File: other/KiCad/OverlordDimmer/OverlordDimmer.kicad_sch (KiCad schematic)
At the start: 61 parts, among them J1 Connector_Screw_Terminal_01x09, J2 USB_cable, J3 RJ45x2, J4 Connector_Screw_Terminal_01x09, J5 USB_B, J6 Conn_01x12_Female, Q21 2N7002E, Q22 2N7002E, Q43 NPN, Q44 BC817, Q45 NPN, U12 4N35, U4 SN65HVD230

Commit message: Finalised ver1.0 revA of PCB
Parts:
- added D18: SBR1A40S1, Diode_SMD:D_SOD-123, symbol Device:D
- Q43, Q45: value NPN -> 2SC4061KT146N
- R12, R13: footprint Resistor_SMD:R_1812_4532Metric_Pad1.30x3.40mm_HandSolder -> Resistor_SMD:R_0402_1005Metric_Pad0.72x0.64mm_HandSolder
- R15, R27: footprint Resistor_SMD:R_0805_2012Metric_Pad1.20x1.40mm_HandSolder -> Resistor_SMD:R_0402_1005Metric_Pad0.72x0.64mm_HandSolder
- R56: footprint Resistor_SMD:R_1210_3225Metric_Pad1.30x2.65mm_HandSolder -> Resistor_SMD:R_0805_2012Metric_Pad1.20x1.40mm_HandSolder
- R60: footprint Resistor_SMD:R_0805_2012Metric_Pad1.20x1.40mm_HandSolder -> Resistor_SMD:R_1210_3225Metric_Pad1.30x2.65mm_HandSolder
- R61: footprint Resistor_SMD:R_0402_1005Metric_Pad0.72x0.64mm_HandSolder -> Resistor_SMD:R_1210_3225Metric_Pad1.30x2.65mm_HandSolder
- R64, R65, R66: footprint Resistor_SMD:R_0805_2012Metric_Pad1.20x1.40mm_HandSolder -> Resistor_SMD:R_1206_3216Metric_Pad1.30x1.75mm_HandSolder
- gave numbers to parts that had none: 1
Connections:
- net at J5.1 (VBUS): now also D18.2 (A); no longer J2.4 (Pin_4)
- new net: D18.1 (K), J2.4 (Pin_4)

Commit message: Final commit from laptop
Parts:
- removed D18: SBR1A40S1, Diode_SMD:D_SOD-123, symbol Device:D
- removed Dbg5V0: Connector_Conn_01x01_Male, Connector_PinHeader_2.54mm:PinHeader_1x01_P2.54mm_Vertical, symbol Overlord-cache:Connector_Conn_01x01_Male
- removed J2: USB_cable, Connector_PinHeader_2.54mm:PinHeader_1x04_P2.54mm_Vertical, symbol Overlord-cache:Connector_Conn_01x04_Male
- removed J3: RJ45x2, Connector_RJ:RJ45_Amphenol_RJHSE538X-02, symbol Overlord-cache:74HC251D,653_RJ45x2
- removed J5: USB_B, Connector_USB:USB_B_OST_USB-B1HSxx_Horizontal, symbol Connector:USB_B
- removed J6: Conn_01x12_Female, Connector_Molex:Molex_CLIK-Mate_502386-1270_1x12-1MP_P1.25mm_Horizontal, symbol Connector_Generic_MountingPin:Conn_01x12_MountingPin
- removed Q21, Q22: 2N7002E, Package_TO_SOT_SMD:SOT-23, symbol Transistor_FET:2N7002E
- removed R27: 5K, Resistor_SMD:R_0402_1005Metric_Pad0.72x0.64mm_HandSolder, symbol Device:R
- removed R30: 10K, Resistor_SMD:R_0805_2012Metric_Pad1.20x1.40mm_HandSolder, symbol Device:R
- added C15, C16: 1uF, Capacitor_SMD:C_0402_1005Metric_Pad0.74x0.62mm_HandSolder, symbol Device:C
- added D18: BZX84C12LT1G, Package_TO_SOT_SMD:SOT-23, symbol Diode:BZX84Cxx
- added D19: 1N4002, Diode_THT:D_DO-41_SOD81_P2.54mm_Vertical_KathodeUp, symbol Device:D
- added J2, J3: DE9_Plug, symbol Connector:DE9_Plug
- added J6: Conn_01x12_Pin, Connector_Molex:Molex_Picoflex_90325-0012_2x06_P1.27mm_Vertical, symbol Connector:Conn_01x12_Pin
- added U13: LM317_SOT-223, Package_TO_SOT_SMD:SOT-223-3_TabPin2, symbol Regulator_Linear:LM317_SOT-223
- R15: value 5K -> 240; footprint Resistor_SMD:R_0402_1005Metric_Pad0.72x0.64mm_HandSolder -> Resistor_SMD:R_1206_3216Metric_Pad1.30x1.75mm_HandSolder
- R25: value 10K -> 390; footprint Resistor_SMD:R_0805_2012Metric_Pad1.20x1.40mm_HandSolder -> Resistor_SMD:R_1206_3216Metric_Pad1.30x1.75mm_HandSolder
- R44, R45, R59, R60, R61, R63: footprint Resistor_SMD:R_1210_3225Metric_Pad1.30x2.65mm_HandSolder -> Resistor_SMD:R_0805_2012Metric_Pad1.20x1.40mm_HandSolder
- R64, R65, R66: footprint Resistor_SMD:R_1206_3216Metric_Pad1.30x1.75mm_HandSolder -> Resistor_SMD:R_0805_2012Metric_Pad1.20x1.40mm_HandSolder
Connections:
- net +12V: now also C15.1, D19.1 (K), J2.6, J3.6, U13.3 (VI); no longer R15.2
- net +3.3V: now also R15.1, C16.1, D19.2 (A), U13.2 (VO)
- net CAN_H: now also J2.7, J3.7, J6.5 (Pin_5)
- net CAN_L: now also J2.2, J3.2, J6.4 (Pin_4)
- net CAN_RX: no longer R25.2
- net GND: now also R25.2, C15.2, C16.2, J2.1, J2.5, J3.1, J3.5, J6.6 (Pin_6)
- net L: now also D14.1 (K); no longer D14.2 (A), J1.4 (Pin_4), J1.6 (Pin_6), J1.8 (Pin_8), J4.5 (Pin_5), J4.7 (Pin_7)
- net N: now also D15.2 (A); no longer D15.1 (K)
- net UART_RX_0: now also J6.8 (Pin_8)
- net UART_TX_0: now also J6.7 (Pin_7)
- net at R65.1: now also J6.2 (Pin_2)
- net at R25.1: now also R15.2, U13.1 (ADJ)
- net at R64.1: now also J6.1 (Pin_1)
- net at R66.1: now also J6.3 (Pin_3)
- net +5V: no longer names the net of ESP1.20 (+5V)
- new net: Q43.1 (B), R60.1, R61.2
- new net: D15.1 (K), Q43.3 (C), R60.2
- new net: D18.3 (K), Q45.1 (B), R61.1
- new net: D14.2 (A), D18.1 (A)
- new net MB1_H: J2.8, J3.8
- new net MB1_L: J2.3, J3.3
- new net MB2_H: J2.9, J3.9
- new net MB2_L: J2.4, J3.4
- no-connect marks 23 -> 27
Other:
- note added: "390 Ohm - 3.3V 680 Ohm - 5V"
- note added: "Power and communication connection"
- note added: "Power conversion"
- note added: "User connection interface"
- note removed: "1 – white/orange - CAN H 2 – orange - CAN L 3 – white/green - x 4 – blue – CAN V+ 5 – white/blue – CAN GND 6 – green - x 7 – white/brown – CAN GND 8 – brown – CAN V+"
- note removed: "1 – white/orange - x 2 – orange - x 3 – white/green - x 4 – blue – +5V 5 – white/blue – GND 6 – green - x 7 – white/brown – x 8 – brown – x"
- note removed: "Connection interface"
- note removed: "POWER connection"
- note removed: "RJ45 power and CAN communication connection"
- note removed: "USB connection"
- moved on the sheet: 11, C4, D15, ESP1, Q43, Q45, R12, R13, R60, R61, U4

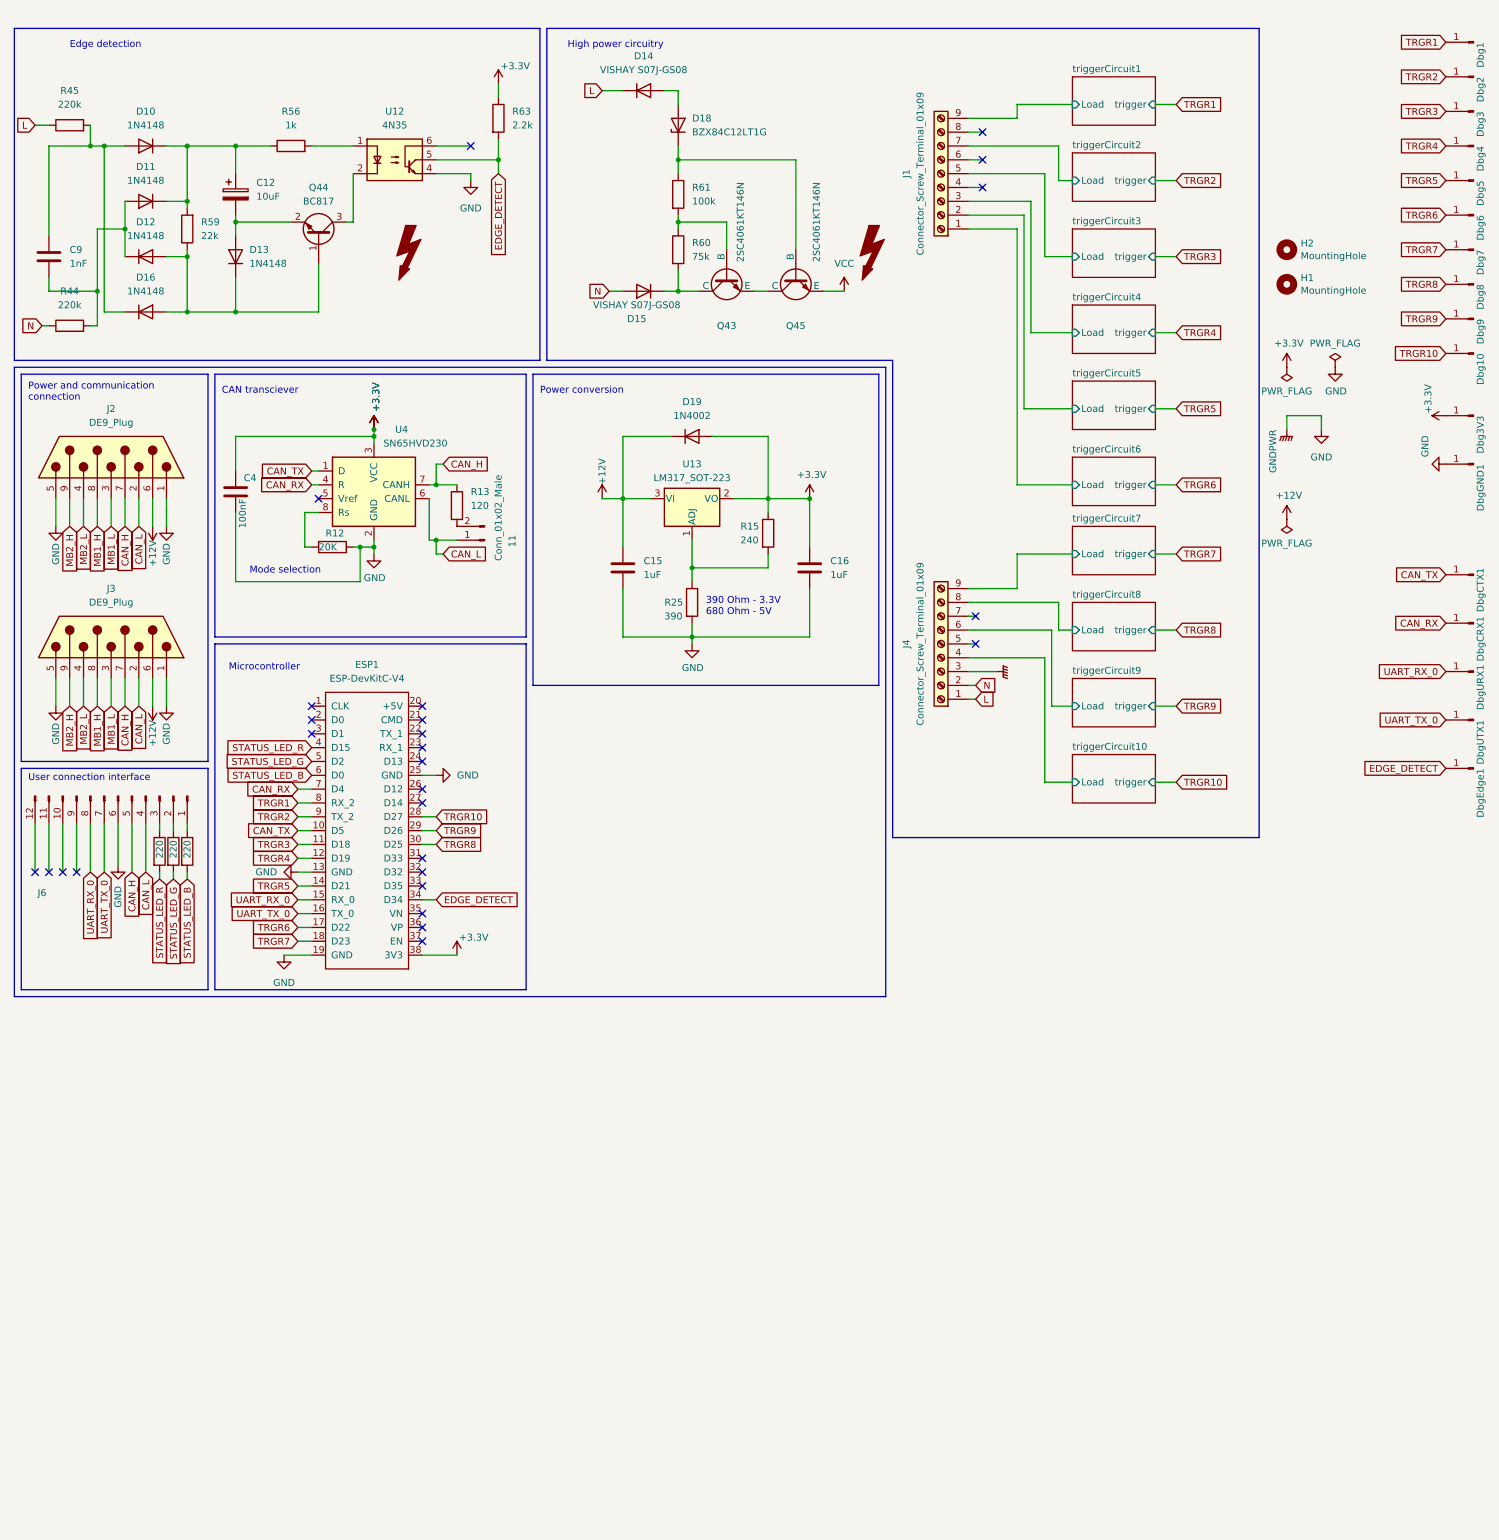
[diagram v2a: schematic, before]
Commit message: uploadable code, serial communication OK TODO: check pin and functionality compatibility
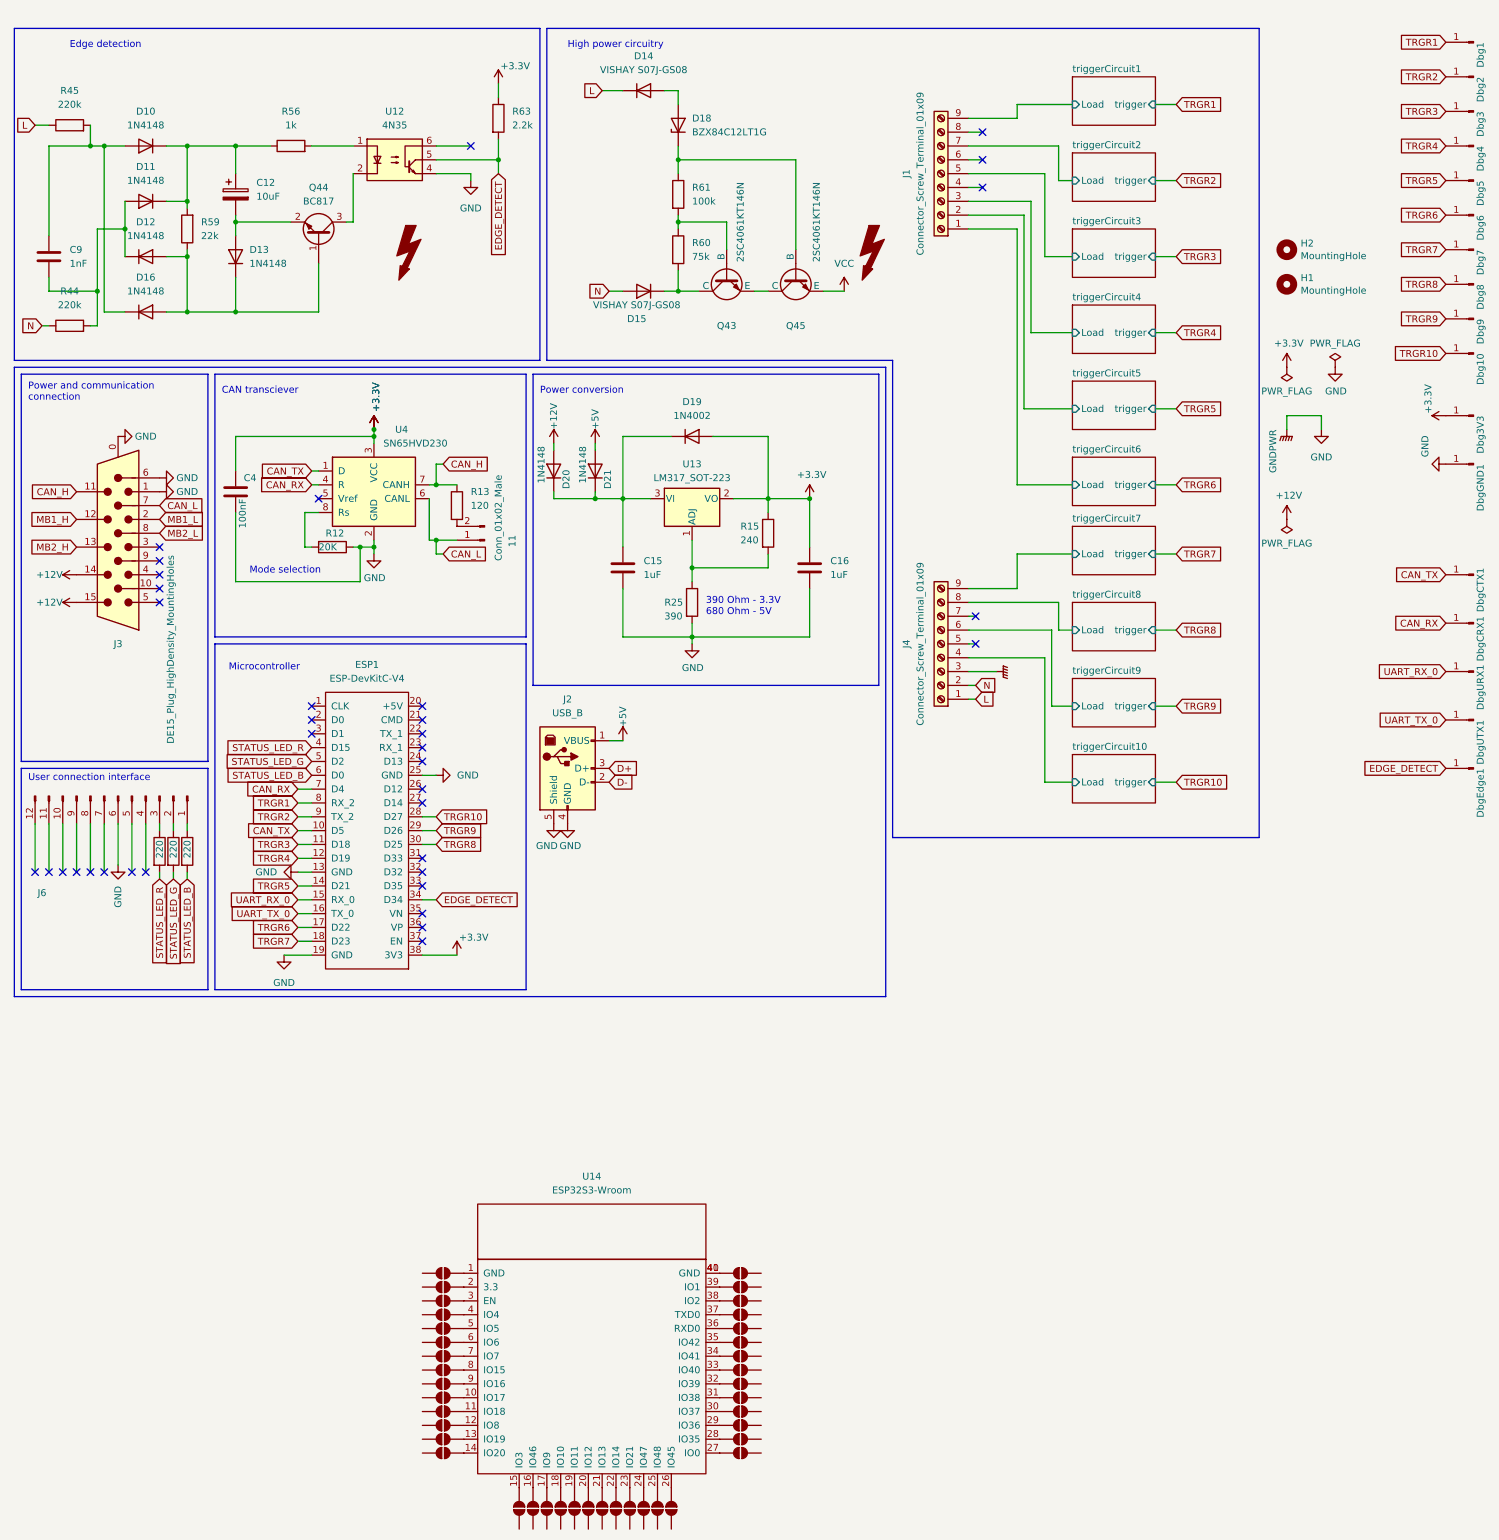
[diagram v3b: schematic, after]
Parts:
- removed J2, J3: DE9_Plug, symbol Connector:DE9_Plug
- added D20, D21: 1N4148, Diode_THT:D_DO-35_SOD27_P7.62mm_Horizontal, symbol Diode:1N4148
- added J2: USB_B, Connector_USB:USB_B_Lumberg_2411_02_Horizontal, symbol Connector:USB_B
- added J3: DE15_Plug_HighDensity_MountingHoles, DSUB-15_Male_Horizontal_P2.77x2.84mm_EdgePinOffset7.70mm_Housed_MountingHolesOffset9.12mm, symbol Connector:DE15_Plug_HighDensity_MountingHoles
- added JP1, JP10, JP11, JP12, JP13, JP14, JP15, JP16, JP17, JP18, JP19, JP2, JP20, JP21, JP22, JP23, JP24, JP25, JP26, JP27, JP28, JP29, JP3, JP30, JP31, JP32, JP33, JP34, JP35, JP36, JP37, JP38, JP39, JP4, JP40, JP5, JP6, JP7, JP8, JP9: SolderJumper_2_Open, Jumper:SolderJumper-2_P1.3mm_Open_RoundedPad1.0x1.5mm, symbol Jumper:SolderJumper_2_Open
- added U14: ESP32S3-Wroom, PCM_Espressif:ESP32-S3-WROOM-1U, symbol ESP32S3-wroom:ESP32S3-Wroom
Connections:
- net +12V: now also D20.2 (A), J3.14, J3.15; no longer C15.1, D19.1 (K), U13.3 (VI)
- net CAN_H: now also J3.11; no longer J6.5 (Pin_5)
- net CAN_L: now also J3.7; no longer J6.4 (Pin_4)
- net GND: now also J2.4 (GND), J2.5 (Shield), J3.0, J3.1, J3.6
- net MB1_H: now also J3.12
- net MB1_L: now also J3.2
- net MB2_H: now also J3.13
- net MB2_L: now also J3.8
- net UART_RX_0: no longer J6.8 (Pin_8)
- net UART_TX_0: no longer J6.7 (Pin_7)
- new net: JP19.1 (A), U14.10 (IO17)
- new net: JP25.1 (A), U14.4 (IO4)
- new net: C15.1, D19.1 (K), D20.1 (K), D21.1 (K), U13.3 (VI)
- new net: JP7.1 (A), U14.34 (IO41)
- new net: JP23.1 (A), U14.6 (IO6)
- new net: JP22.1 (A), U14.7 (IO7)
- new net: JP6.1 (A), U14.35 (IO42)
- new net: JP5.1 (A), U14.36 (RXD0)
- new net: JP3.1 (A), U14.38 (IO2)
- new net: JP28.1 (A), U14.1 (GND)
- new net: JP18.1 (A), U14.11 (IO18)
- new net: JP17.1 (A), U14.12 (IO8)
- new net: JP16.1 (A), U14.13 (IO19)
- new net: JP15.1 (A), U14.14 (IO20)
- new net: JP40.1 (A), U14.15 (IO3)
- new net: JP39.1 (A), U14.16 (IO46)
- new net: JP38.1 (A), U14.17 (IO9)
- new net: JP37.1 (A), U14.18 (IO10)
- new net: JP36.1 (A), U14.19 (IO11)
- new net: JP27.1 (A), U14.2 (3.3)
- new net: JP35.1 (A), U14.20 (IO12)
- new net: JP34.1 (A), U14.21 (IO13)
- new net: JP33.1 (A), U14.22 (IO14)
- new net: JP32.1 (A), U14.23 (IO21)
- new net: JP31.1 (A), U14.24 (IO47)
- new net: JP30.1 (A), U14.25 (IO48)
- new net: JP29.1 (A), U14.26 (IO45)
- new net: JP14.1 (A), U14.27 (IO0)
- new net: JP13.1 (A), U14.28 (IO35)
- new net: JP12.1 (A), U14.29 (IO36)
- new net: JP26.1 (A), U14.3 (EN)
- new net: JP11.1 (A), U14.30 (IO37)
- new net: JP10.1 (A), U14.31 (IO38)
- new net: JP9.1 (A), U14.32 (IO39)
- new net: JP8.1 (A), U14.33 (IO40)
- new net: JP4.1 (A), U14.37 (TXD0)
- new net: JP2.1 (A), U14.39 (IO1)
- new net: JP1.1 (A), U14.40 (GND), U14.41 (GND)
- new net: JP24.1 (A), U14.5 (IO5)
- new net: JP21.1 (A), U14.8 (IO15)
- new net: JP20.1 (A), U14.9 (IO16)
- new net +5V: D21.2 (A), J2.1 (VBUS)
- new net D+: J2.3 (D+)
- new net D-: J2.2 (D-)
- no-connect marks 27 -> 36
